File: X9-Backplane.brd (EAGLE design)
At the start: 122.1 x 122.1 mm, 8 parts

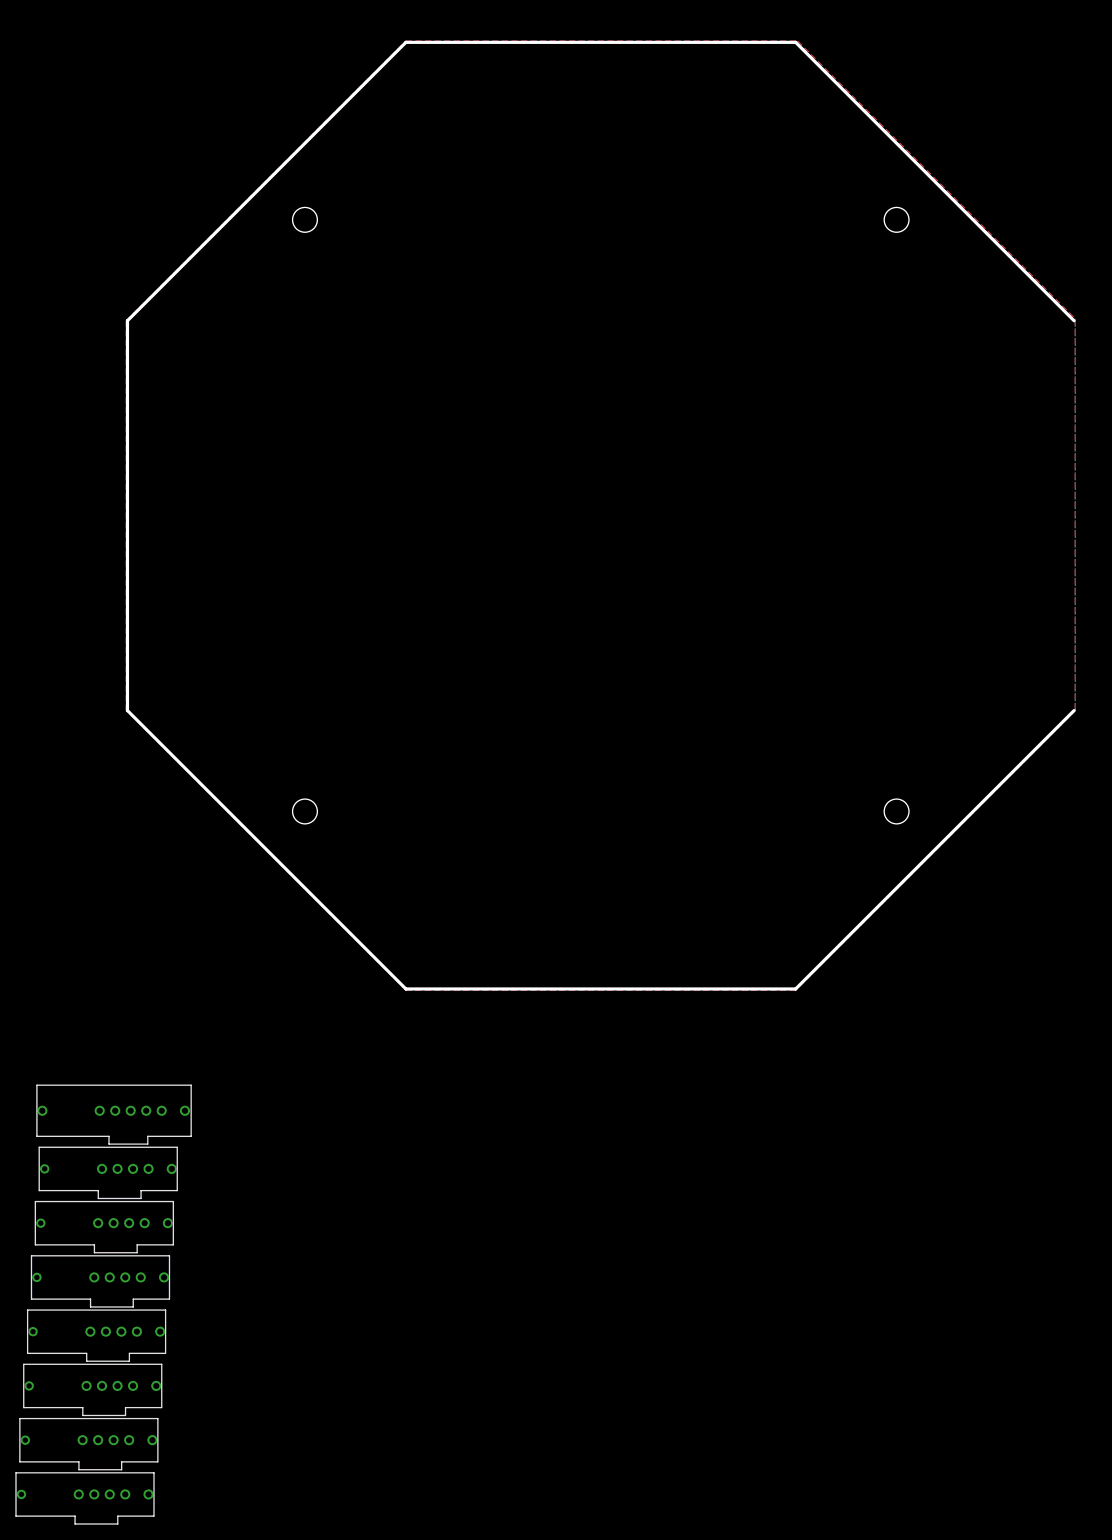
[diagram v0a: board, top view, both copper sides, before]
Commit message: created the backplane
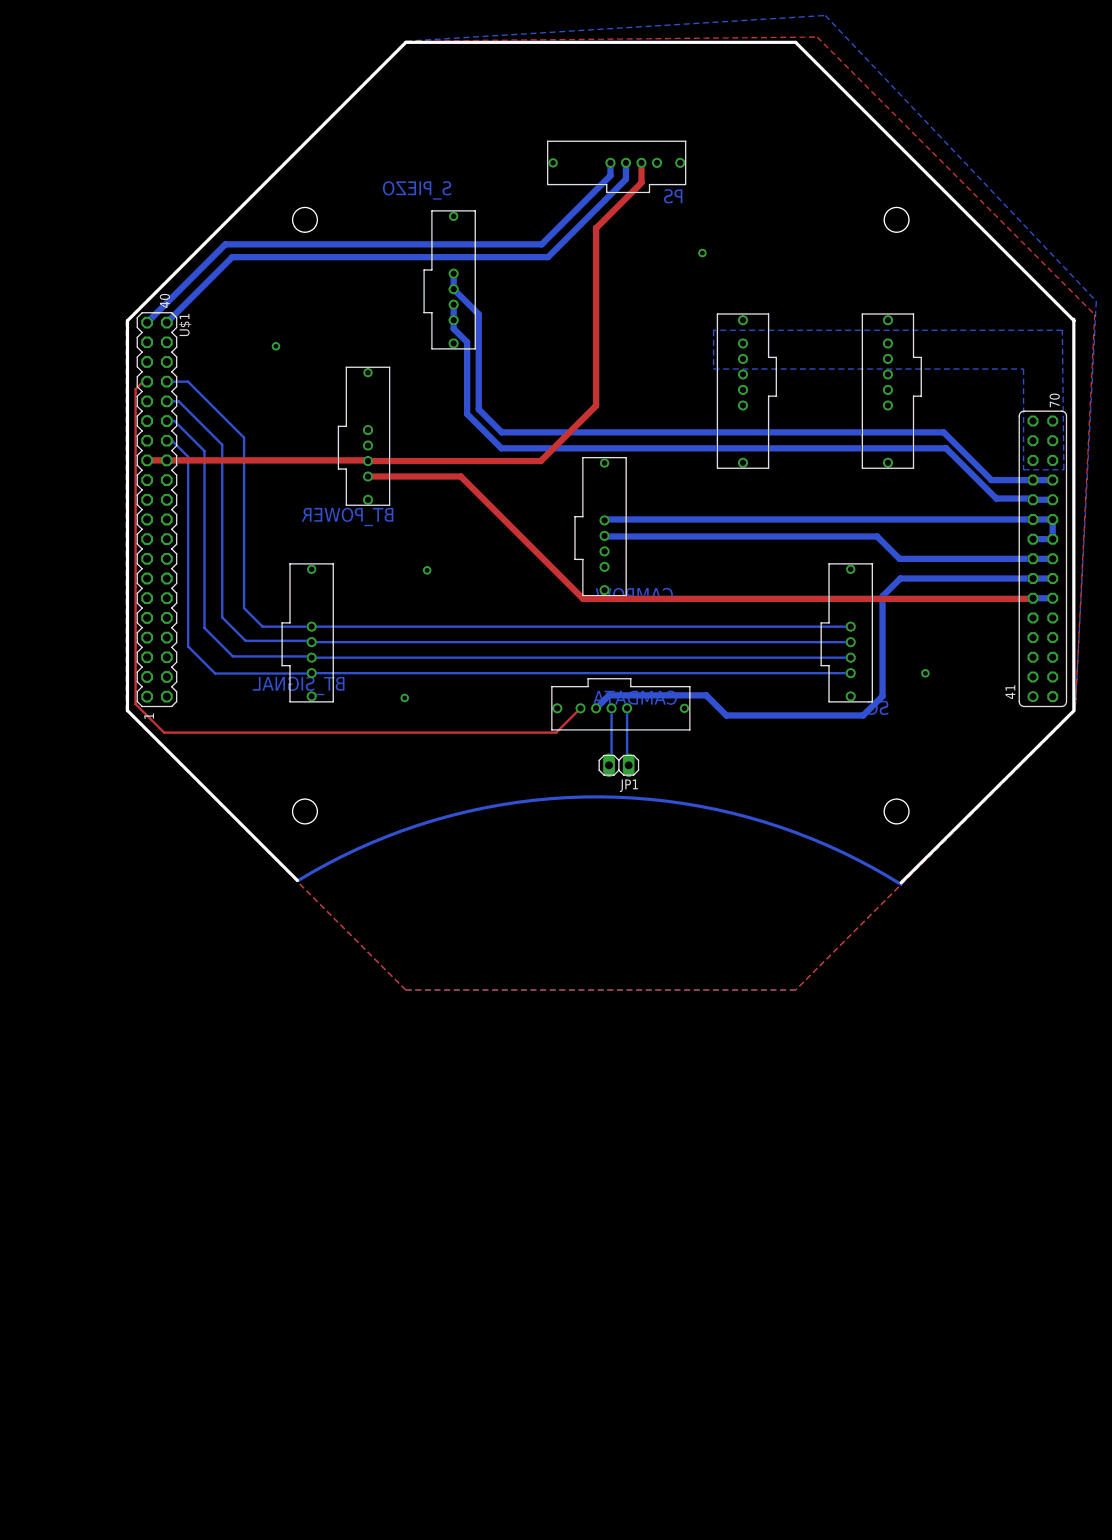
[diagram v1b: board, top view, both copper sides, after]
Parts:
- removed ETHERNET, I2C, SC1, SC2: T2I, BACKPLANE:T2I
- added BT_POWER, BT_SIGNAL, SC, S_PIEZO: T2I, BACKPLANE:T2I
- added JP1: (no value), pinhead:1X02
- added POWER1: T2I5P, T2I5P:T2I5P
- added U$1: SHIELDCONNECTOR, backplane_to_shield_connector:20X2PIN
- moved PS 185.0 mm to (53.6, 79.8)
- moved POWER 129.6 mm to (82.1, 63.0), turned to 90 degrees
- moved CAMPOW 123.7 mm to (58.1, 44.6), turned to 270 degrees
- moved CAMDATA 106.2 mm to (71.9, 15.0), turned to 180 degrees
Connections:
- removed net 1H: ETHERNET.1
- removed net 1L: ETHERNET.2
- removed net 2H: ETHERNET.3
- removed net 2L: ETHERNET.4
- removed net 5V: CAMPOW.1, SC1.3, SC2.3
- removed net D+/S1: SC1.1
- removed net D+/S2: SC2.1
- removed net D-/S1: SC1.2
- removed net D-/S2: SC2.2
- removed net LED: CAMDATA.3
- removed net SCL/H: I2C.1
- removed net SCL/L: I2C.2
- removed net SDA/H: I2C.3
- removed net SDA/L: I2C.4
- removed net SERVO: CAMDATA.4
- new net +12V: POWER.P$5, POWER.P$6, POWER1.P$5, POWER1.P$6, U$1.65, U$1.66, U$1.67, U$1.68, U$1.69, U$1.70
- new net 3V3_PIEZO: S_PIEZO.1, S_PIEZO.2, U$1.63, U$1.64
- new net 5V_BT_LED: BT_POWER.4, U$1.51, U$1.52
- new net 5V_CAMERA_TUBE: CAMPOW.1, U$1.57, U$1.58, U$1.59, U$1.60
- new net 5V_LASER: CAMPOW.2, U$1.55, U$1.56
- new net 5V_LED: CAMDATA.3, U$1.53, U$1.54
- new net DSCLM: U$1.36
- new net DSDAM: U$1.38
- new net DSDAP: U$1.37
- new net DSDLP: U$1.35
- new net GND_PIEZO: S_PIEZO.3, S_PIEZO.4, U$1.61, U$1.62
- new net N$23: POWER.P$4
- new net N$28: POWER1.P$4
- new net RX_H: BT_SIGNAL.3, SC.3, U$1.30
- new net RX_L: BT_SIGNAL.4, SC.4, U$1.28
- new net SERVO_PWM: CAMDATA.4, U$1.33
- new net TX_H: BT_SIGNAL.1, SC.1, U$1.34
- new net TX_L: BT_SIGNAL.2, SC.2, U$1.32
- net 3.3V: now also BT_POWER.3, U$1.25, U$1.26; no longer CAMPOW.2
- net D+: now also JP1.1
- net D-: now also JP1.2
- net GND: now also BT_POWER.1, BT_POWER.2, POWER.P$2, POWER.P$3, POWER1.P$2, POWER1.P$3, U$1.1, U$1.2, U$1.3, U$1.4, U$1.41, U$1.42, U$1.43, U$1.44, U$1.45, U$1.46, U$1.47, U$1.48, U$1.49, U$1.50; no longer SC1.4, SC2.4
- net SCL: now also U$1.39
- net SDA: now also U$1.40
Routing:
- net RX_L: track 0.00 -> 115.0 mm
- net RX_H: track 0.00 -> 114.3 mm
- net TX_H: track 0.00 -> 114.2 mm
- net TX_L: track 0.00 -> 114.2 mm
- net SERVO_PWM: track 0.00 -> 102.7 mm
- net 3V3_PIEZO: track 0.00 -> 96.7 mm
- net GND_PIEZO: track 0.00 -> 95.0 mm
- net 5V_BT_LED: track 0.00 -> 94.9 mm
- net 3.3V: track 0.00 -> 94.7 mm
- net N$21: track 0.00 -> 77.8 mm
- net 5V_LED: track 0.00 -> 75.5 mm
- net SCL: track 0.00 -> 69.3 mm
- net SDA: track 0.00 -> 69.0 mm
- net 5V_CAMERA_TUBE: track 0.00 -> 63.0 mm
- net 5V_LASER: track 0.00 -> 59.0 mm
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- added copper zone on layer 16, net +12V
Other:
- board size 122.1 x 122.1 mm -> 122.1 x 108.4 mm
- board text added: "BT_POWER"
- board text added: "BT_SIGNAL"
- board text added: "CAMDATA"
- board text added: "CAMPOW"
- board text added: "MAIN_POWER"
- board text added: "PS"
- board text added: "SC"
- board text added: "S_PIEZO"

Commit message: resizing the board
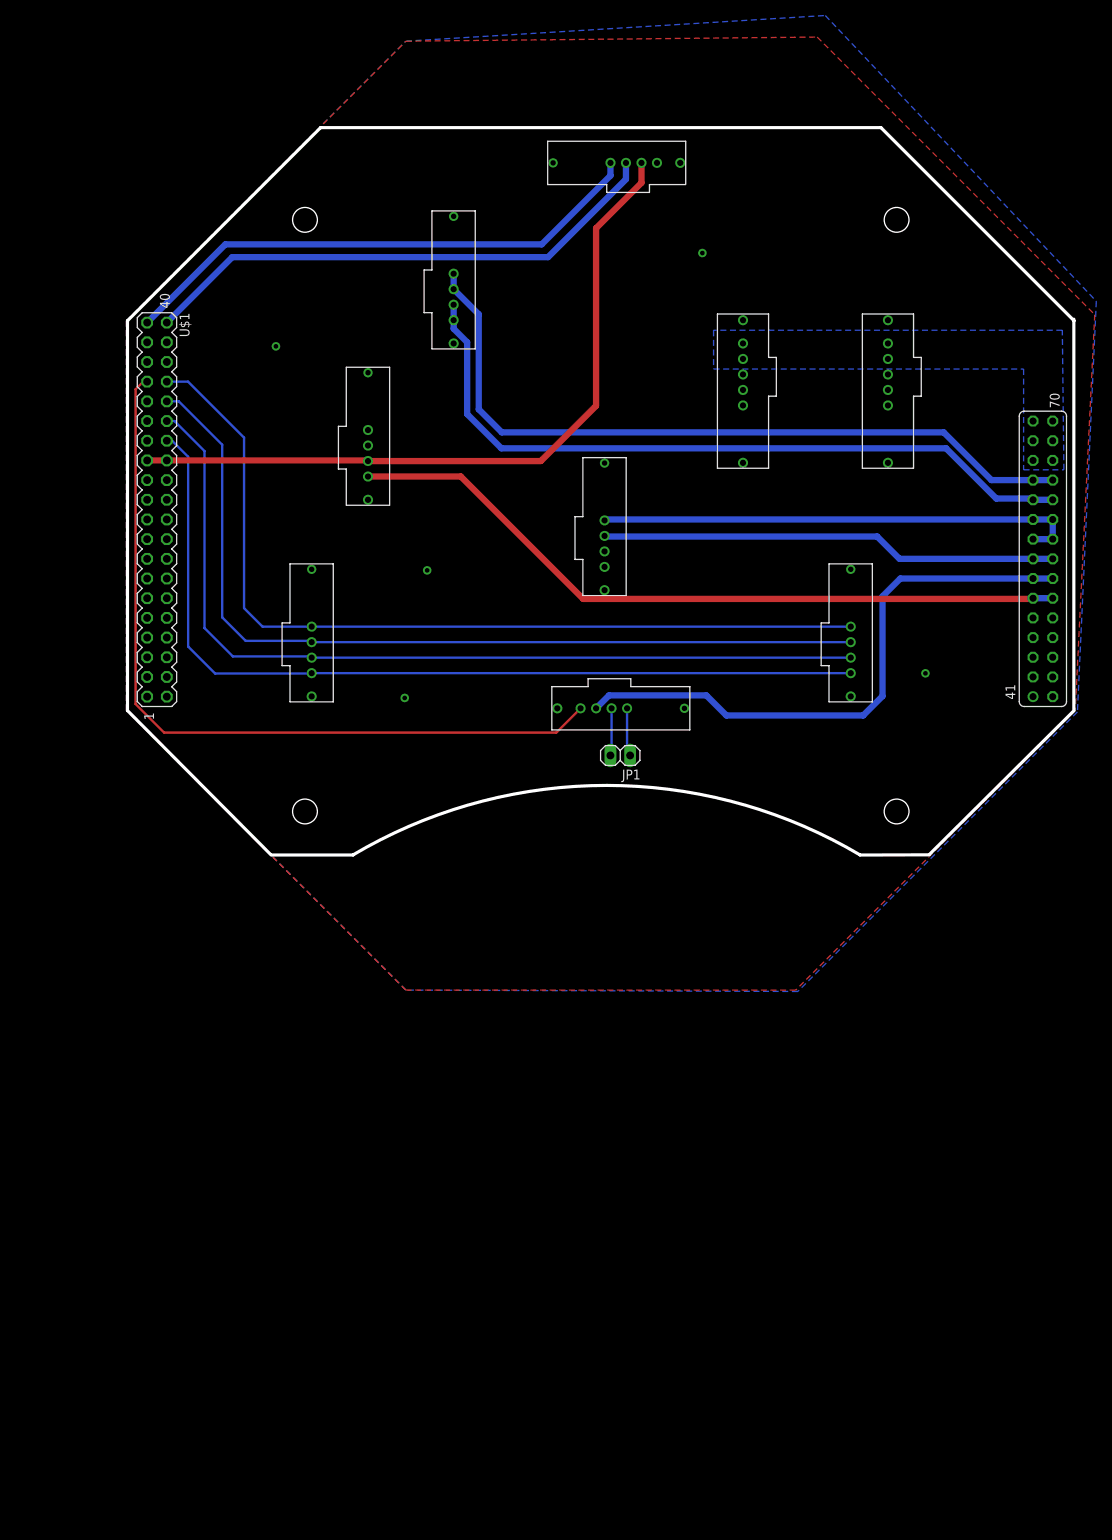
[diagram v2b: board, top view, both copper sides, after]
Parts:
- moved JP1 1.28 mm to (63.0, 6.14)
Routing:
- net N$21: track 77.8 -> 0.00 mm
- net D-: track 7.49 -> 6.11 mm
- net D+: track 7.44 -> 6.15 mm
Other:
- board size 122.1 x 108.4 mm -> 122.1 x 93.9 mm
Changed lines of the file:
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@@
 <setting verticaltext="up"/>
 </settings>
-<grid distance="1" unitdist="mil" unit="mil" style="lines" multiple="1" display="yes" altdistance="0.025" altunitdist="inch" altunit="inch"/>
+<grid distance="1" unitdist="mm" unit="mm" style="lines" multiple="1" display="yes" altdistance="0.025" altunitdist="inch" altunit="inch"/>
 <layers>
 <layer number="1" name="Top" color="4" fill="1" visible="no" active="yes"/>
@@
 <hole x="98.616953125" y="75.247665625" drill="3.2"/>
 <circle x="60.45086875" y="37.08158125" radius="73.025" width="0.4064" layer="51"/>
-<wire x1="35.30615" y1="98.14731875" x2="-0.614875" y2="62.22629375" width="0.4064" layer="20"/>
-<wire x1="121.51660625" y1="11.9368625" x2="99.195584375" y2="-10.2841625" width="0.4064" layer="20"/>
-<wire x1="-0.614875" y1="11.9368625" x2="21.30615" y2="-9.9841625" width="0.4064" layer="20"/>
-<wire x1="85.595584375" y1="98.14731875" x2="121.51660625" y2="62.22629375" width="0.4064" layer="20"/>
-<wire x1="85.595584375" y1="98.14731875" x2="35.30615" y2="98.14731875" width="0.4064" layer="20"/>
+<wire x1="24.30615" y1="87.14731875" x2="-0.614875" y2="62.22629375" width="0.4064" layer="20"/>
+<wire x1="121.51660625" y1="11.9368625" x2="102.827784375" y2="-6.6519625" width="0.4064" layer="20"/>
+<wire x1="-0.614875" y1="11.9368625" x2="17.87715" y2="-6.6567625" width="0.4064" layer="20"/>
+<wire x1="96.595584375" y1="87.14731875" x2="121.51660625" y2="62.22629375" width="0.4064" layer="20"/>
 <wire x1="-0.614875" y1="62.22629375" x2="-0.614875" y2="11.9368625" width="0.4064" layer="20"/>
 <text x="80.1" y="70.4" size="1.778" layer="22" rot="MR0">MAIN_POWER</text>
 <text x="98.8" y="72.9" size="1.778" layer="22" rot="MR0">MAIN_POWER</text>
 <wire x1="121.485125" y1="62.42629375" x2="121.485125" y2="12.1368625" width="0.4064" layer="20"/>
-<text x="33.9" y="36.3" size="1.778" layer="16" rot="MR0">BT_POWER</text>
-<text x="27.6" y="14.5" size="1.778" layer="16" rot="MR0">BT_SIGNAL</text>
-<text x="69.881" y="25.9566" size="1.778" layer="16" rot="MR0">CAMPOW</text>
-<text x="70.4" y="12.7" size="1.778" layer="16" rot="MR0">CAMDATA</text>
-<text x="71.2" y="77.4" size="1.778" layer="16" rot="MR0">PS</text>
-<text x="41.2954" y="78.4302" size="1.778" layer="16" rot="MR0">S_PIEZO</text>
-<text x="97.7" y="11.4" size="1.778" layer="16" rot="MR0">SC</text>
+<text x="33.9" y="36.3" size="1.778" layer="22" rot="MR0">BT_POWER</text>
+<text x="27.6" y="14.5" size="1.778" layer="22" rot="MR0">BT_SIGNAL</text>
+<text x="69.881" y="25.9566" size="1.778" layer="22" rot="MR0">CAMPOW</text>
+<text x="70.4" y="12.7" size="1.778" layer="22" rot="MR0">CAMDATA</text>
+<text x="71.2" y="77.4" size="1.778" layer="22" rot="MR0">PS</text>
+<text x="41.2954" y="78.4302" size="1.778" layer="22" rot="MR0">S_PIEZO</text>
+<text x="97.7" y="11.4" size="1.778" layer="22" rot="MR0">SC</text>
+<wire x1="96.595584375" y1="87.14731875" x2="24.30615" y2="87.14731875" width="0.4064" layer="20"/>
+<wire x1="28.496384375" y1="-6.70388125" x2="17.95795" y2="-6.70388125" width="0.4064" layer="20"/>
+<wire x1="102.791384375" y1="-6.67848125" x2="93.90395" y2="-6.70388125" width="0.4064" layer="20"/>
+<wire x1="28.4988" y1="-6.6802" x2="93.8784" y2="-6.6802" width="0.4064" layer="20" curve="-61.297013"/>
 </plain>
 <attributes>
@@
 <element name="BT_POWER" library="BACKPLANE" package="T2I" value="T2I" x="27.6172" y="56.2294" rot="R270"/>
 <element name="U$1" library="backplane_to_shield_connector" package="20X2PIN" value="SHIELDCONNECTOR" x="57.8" y="40.4"/>
-<element name="JP1" library="pinhead" package="1X02" value="" x="62.784" y="4.8726" rot="R180"/>
+<element name="JP1" library="pinhead" package="1X02" value="" x="62.9618" y="6.1426" rot="R180"/>
 </elements>
 <signals>
@@
 <vertex x="89.4158" y="101.6126"/>
 <vertex x="124.3838" y="64.7446"/>
-<vertex x="121.666" y="11.938"/>
-<vertex x="85.598" y="-24.13"/>
+<vertex x="121.9454" y="11.7602"/>
+<vertex x="85.8774" y="-24.3078"/>
 <vertex x="35.306" y="-24.13"/>
 <vertex x="-0.762" y="11.938"/>
@@
 <contactref element="CAMDATA" pad="1"/>
 <contactref element="JP1" pad="1"/>
-<wire x1="63.843" y1="12.2232" x2="63.843" y2="5.0836" width="0.3048" layer="16"/>
-<wire x1="63.843" y1="5.0836" x2="64.054" y2="4.8726" width="0.3048" layer="16"/>
+<wire x1="63.843" y1="12.2232" x2="63.843" y2="7.2426" width="0.3048" layer="16"/>
+<wire x1="63.843" y1="7.2426" x2="64.2318" y2="6.1426" width="0.3048" layer="16"/>
 </signal>
 <signal name="D-">
 <contactref element="CAMDATA" pad="2"/>
 <contactref element="JP1" pad="2"/>
-<wire x1="61.843" y1="12.2232" x2="61.843" y2="5.2016" width="0.3048" layer="16"/>
-<wire x1="61.843" y1="5.2016" x2="61.514" y2="4.8726" width="0.3048" layer="16"/>
+<wire x1="61.843" y1="12.2232" x2="61.843" y2="6.4716" width="0.3048" layer="16"/>
+<wire x1="61.843" y1="6.4716" x2="61.6918" y2="6.1426" width="0.3048" layer="16"/>
 </signal>
 <signal name="5V_LED">
@@
 </signal>
 <signal name="N$21">
-<wire x1="21.4" y1="-10" x2="99.2" y2="-10.5" width="0.4064" layer="16" curve="-63.42779"/>
 </signal>
 <signal name="DSDAP">
